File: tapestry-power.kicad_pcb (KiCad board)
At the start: 2 copper layers, 15 parts, among them J1 4.5-20V, J2 4.5-20V, J3 5V, U1 sic450

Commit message: basic board
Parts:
- L1: footprint Inductor_SMD:L_12x12mm_H6mm -> libs:IP67GZ01
- moved J1 13.8 mm to (119.3, 68.1)
- moved J2 9.77 mm to (112.4, 55.3)
- moved J3 5.64 mm to (169.9, 67.1)
- moved L1 3.51 mm to (154.7, 64.3)
- moved C1 2.55 mm to (142.1, 61.8)
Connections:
- net Net-(L1-Pad1) renamed /VHIGH
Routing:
- net /VOUT: track 8.88 -> 38.1 mm, vias 0 -> 2
- net /VIN: track 5.38 -> 21.7 mm, vias 0 -> 2
- net GND: vias 0 -> 82
- added copper zone on F.Cu, net /VHIGH
- added copper zone on F.Cu, net /VIN
- added copper zone on F.Cu, net /VOUT
- added copper zone on B.Cu, net GND
- added copper zone on F.Cu, net GND
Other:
- board outline added: 73.7 x 25.4 mm

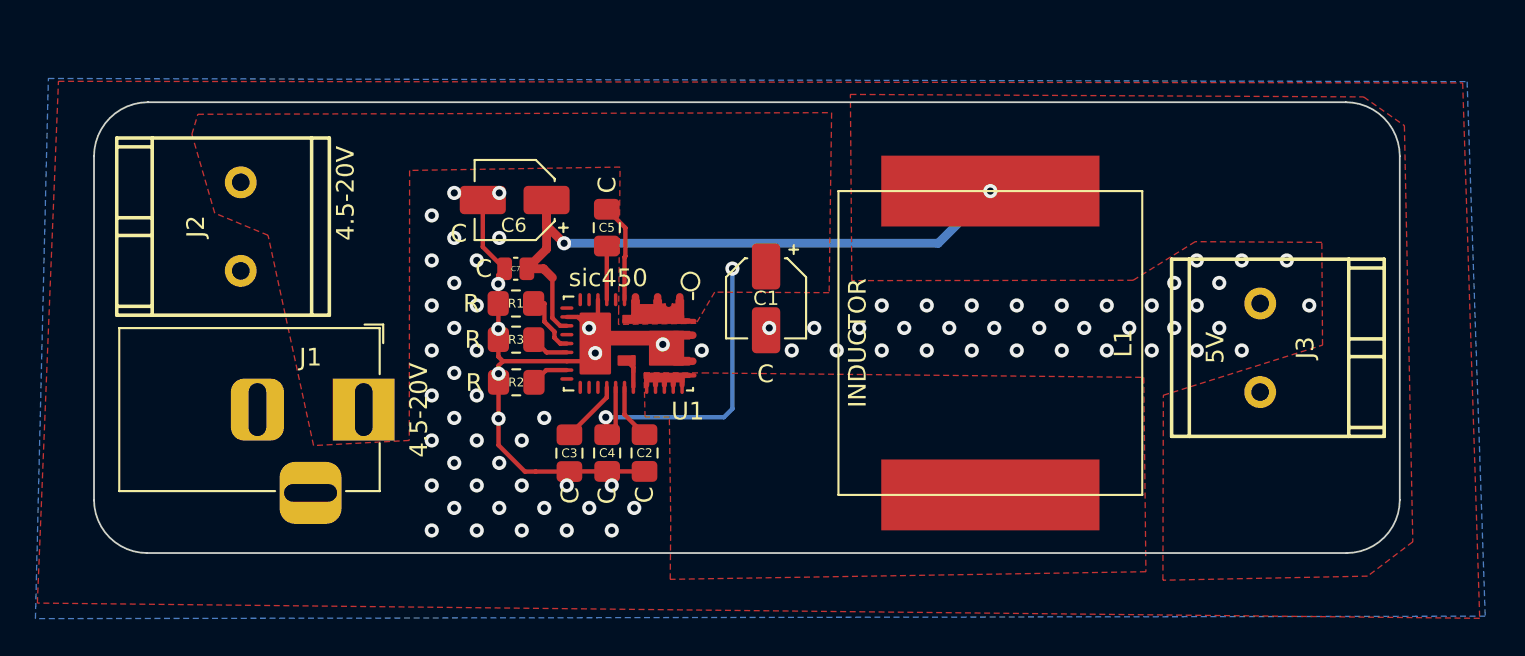
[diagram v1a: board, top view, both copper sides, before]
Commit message: Tightened up pours.  Added Fiducials
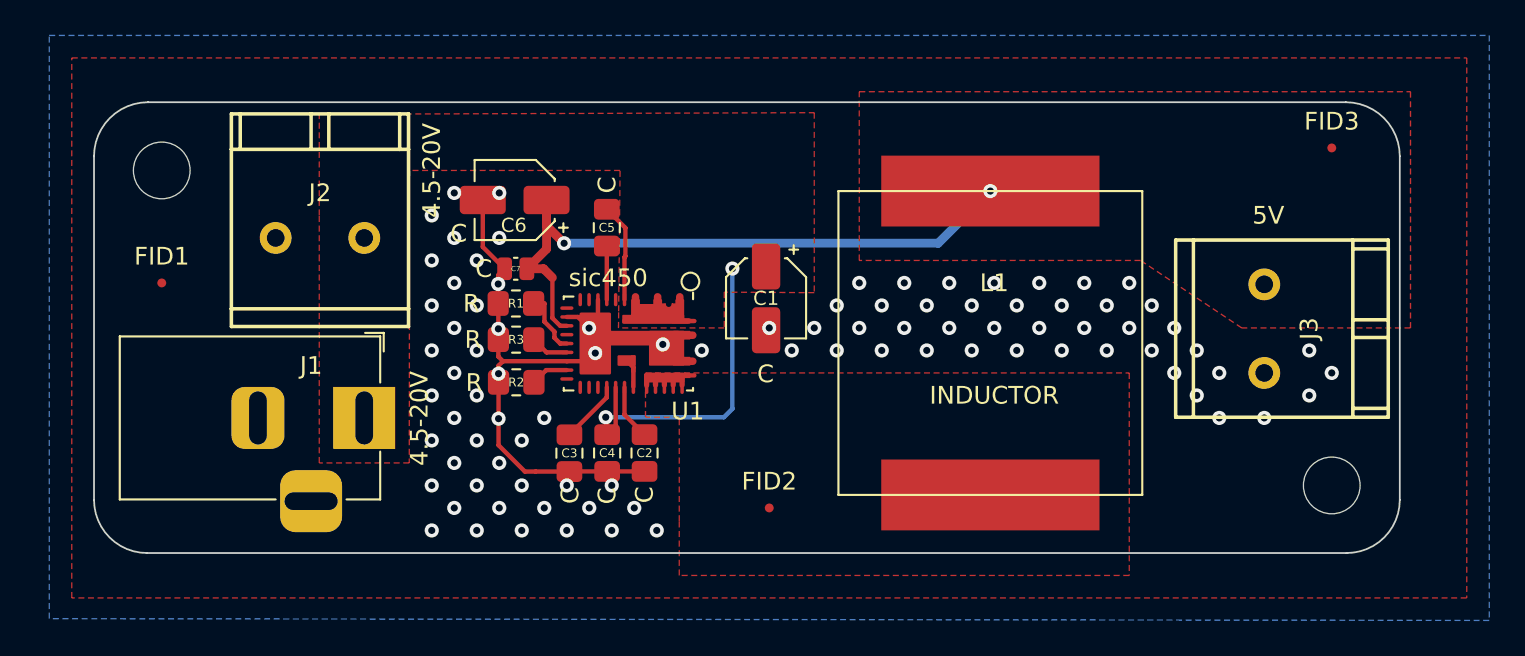
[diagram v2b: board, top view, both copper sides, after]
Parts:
- added FID1: Fiducial, Fiducial:Fiducial_0.5mm_Mask1mm, F.Cu at (108.0, 61.0)
- added FID2: Fiducial, Fiducial:Fiducial_0.5mm_Mask1mm, F.Cu at (142.2, 73.7)
- added FID3: Fiducial, Fiducial:Fiducial_0.5mm_Mask1mm, F.Cu at (174.0, 53.3)
- added H1: MountingHole, MountingHole:MountingHole_3.2mm_M3, F.Cu at (108.0, 54.6)
- added H2: MountingHole, MountingHole:MountingHole_3.2mm_M3, F.Cu at (174.0, 72.4)
- added H3: HoP Graphic, libs:HoP_logo, B.Cu at (160.0, 63.5)
- moved J2 7.64 mm to (119.4, 58.4), turned to 180 degrees
- moved J3 1.10 mm to (170.2, 66.0)
- moved J1 0.47 mm to (119.4, 68.6)
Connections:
- J3 pad 1: /VOUT -> GND
- J3 pad 2: GND -> /VOUT
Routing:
- net GND: vias 82 -> 90
